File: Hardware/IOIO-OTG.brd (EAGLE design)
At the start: 68.6 x 30.5 mm, 51 parts, among them Q1 IRLML2244, Q2 2N7002PW, U1 PIC24FJ256GB206, U14 SWITCH_SPDT, U2 TPS6214X"", U3 VREG_MIC5216

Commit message: Consistency fixes
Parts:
- C10: device SparkFun-Passives:EIA3216 -> SparkFun-Capacitors:EIA3216
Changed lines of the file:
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@@
 <attribute name="VALUE" x="32.0997" y="20.221653125" size="0.4064" layer="27" rot="R45"/>
 </element>
-<element name="C10" library="SparkFun-Passives" package="EIA3216" value="10uF" x="38.1" y="21.59" smashed="yes" rot="R270">
+<element name="C10" library="SparkFun-Capacitors" package="EIA3216" value="10uF" x="38.1" y="21.59" smashed="yes" rot="R270">
 <attribute name="NAME" x="39.481" y="24.13" size="0.4064" layer="25" rot="R270"/>
 <attribute name="VALUE" x="39.432" y="21.182" size="0.4064" layer="27" rot="R270"/>

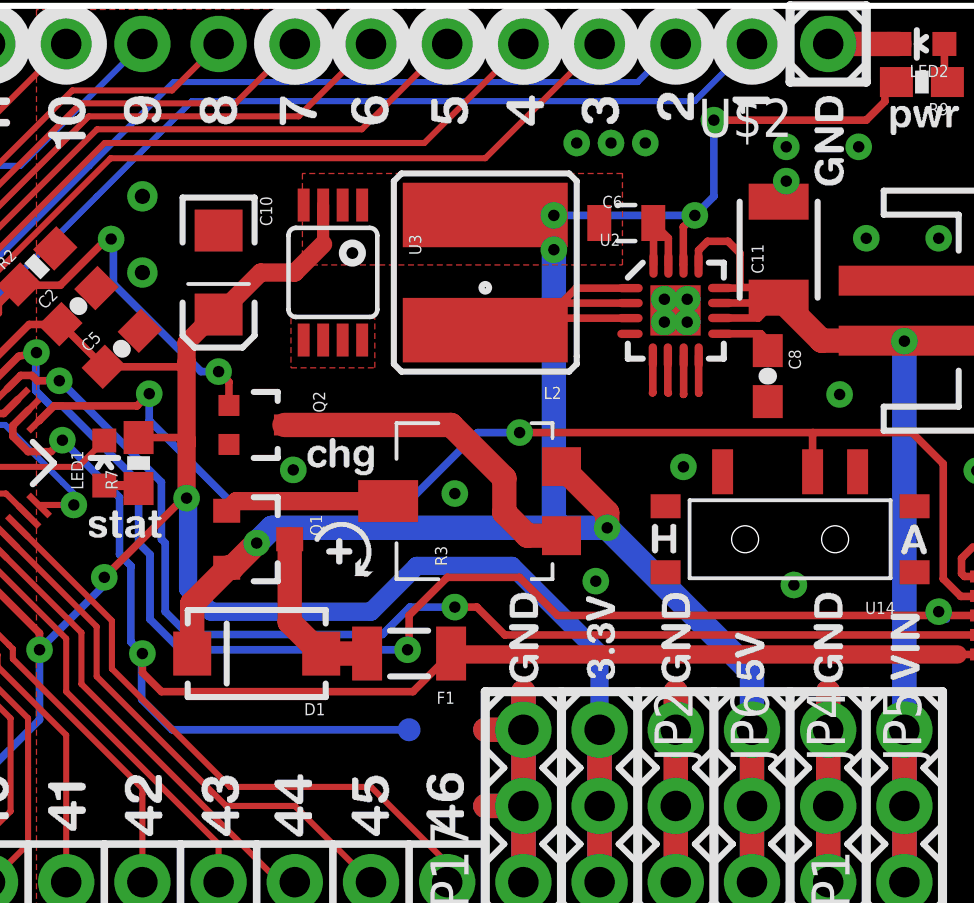
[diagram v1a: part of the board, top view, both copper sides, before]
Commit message: Final 6.5.0 inconsistency fixes
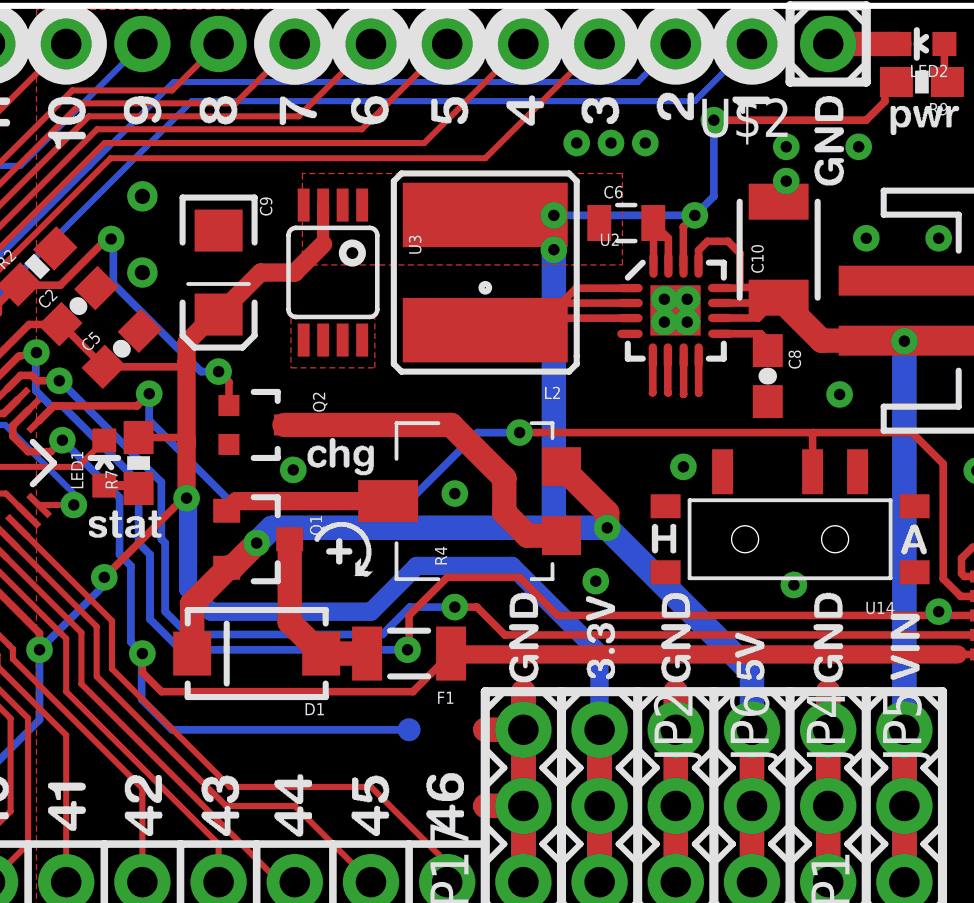
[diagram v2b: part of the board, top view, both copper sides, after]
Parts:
- removed C11: 10uF, SparkFun-Passives:1210
- added C9: 10uf, SparkFun-Capacitors:EIA3216
- C10: value 10uF -> 10uf; device SparkFun-Capacitors:EIA3216 -> SparkFun-Passives:1210
- C6: value 10uF -> 10uf
- D1: value B340A -> DIODE-SCHOTTKY_
- Q2: value 2N7002PW -> MOSFET-NCHANNEL2N7002PW"; device SparkFun-DiscreteSemi:SOT323 -> SparkFun-DiscreteSemi:SOT323_NOAT
- R4: value TS53YL502MR10 -> TRIMPOTSMD_STANDARD
- moved C10 18.7 mm to (56.8, 22.4), turned to 90 degrees
- renumbered R3 to R4
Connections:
- net 3.3V: now also C9.A; no longer C10.A
- net GND: now also C10.2, C9.C; no longer C10.C, C11.2
- net VIN: now also C10.1; no longer C11.1
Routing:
- net VIN: track 37.7 -> 38.7 mm

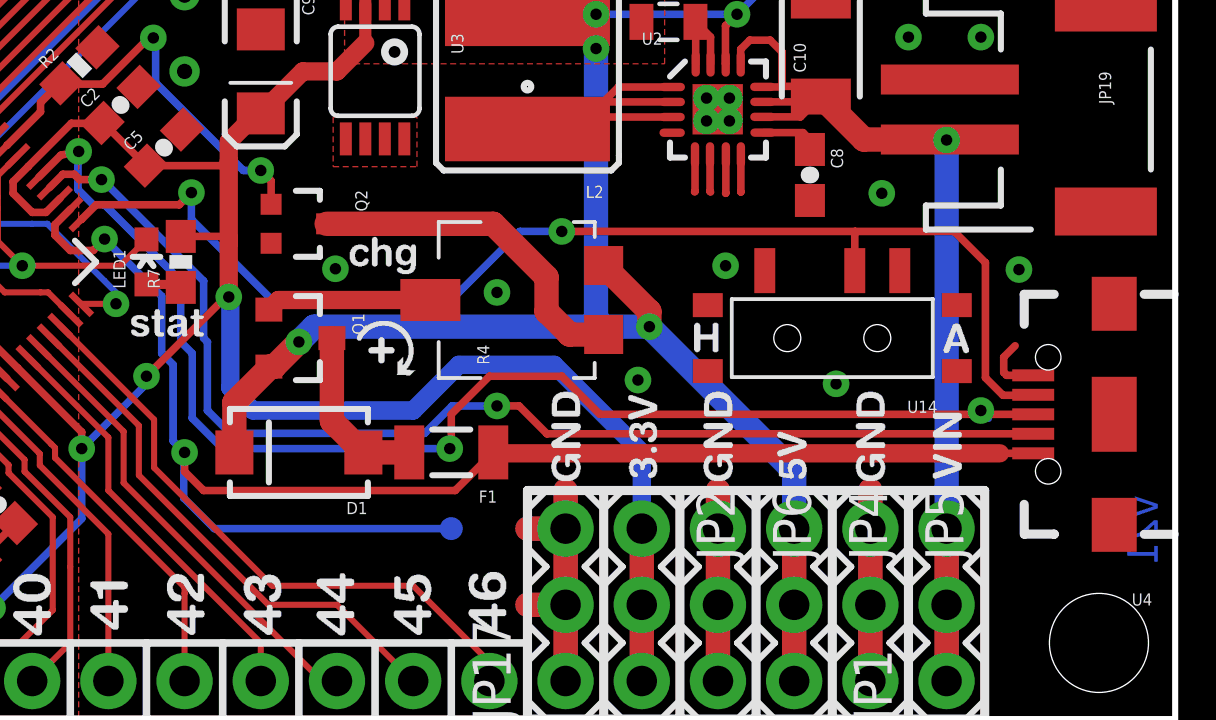
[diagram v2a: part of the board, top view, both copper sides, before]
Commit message: Added test-points
3 new test-points:
D+
D-
USBID
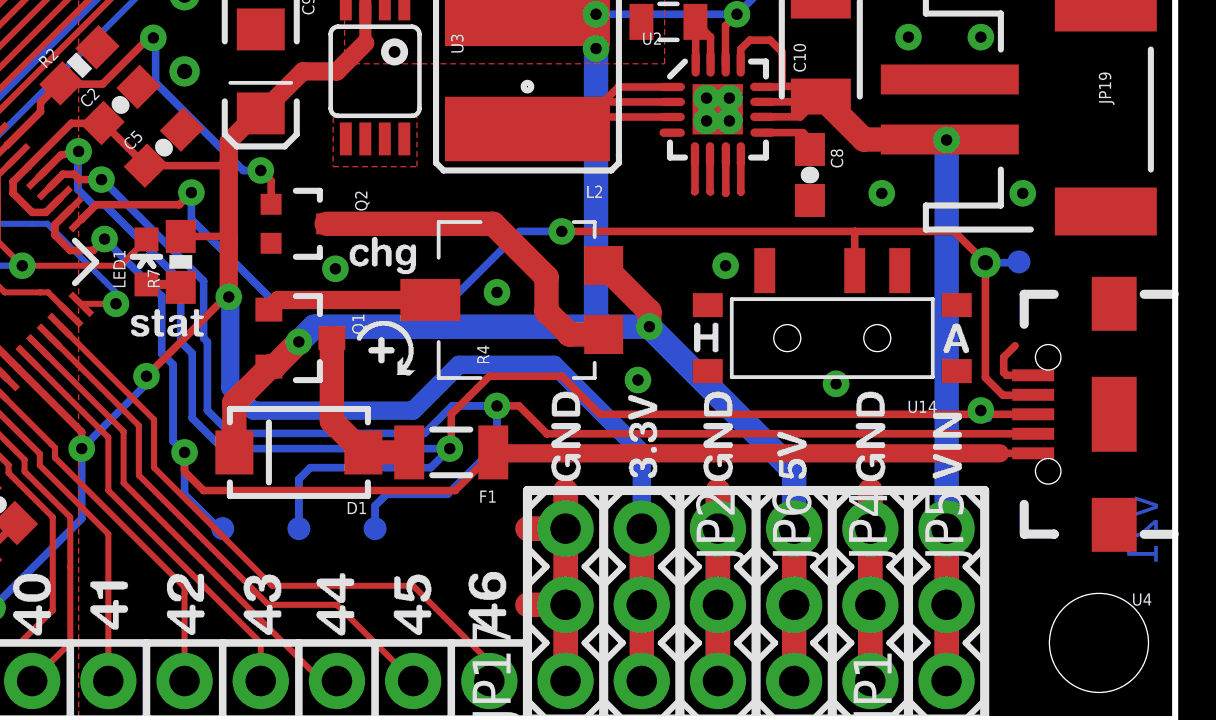
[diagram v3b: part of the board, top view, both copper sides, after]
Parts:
- added TP2, TP3, TP4: TEST-POINT3, SparkFun-Passives:PAD.03X.03
- moved TP1 7.62 mm to (36.8, 6.35)
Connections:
- net D+: now also TP3.P$1
- net D-: now also TP2.P$1
- net USBID: now also TP4.P$1
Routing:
- net VBUS: track 52.0 -> 44.2 mm
- net D+: track 43.4 -> 50.5 mm
- net D-: track 39.8 -> 46.7 mm
- net USBID: track 40.9 -> 42.0 mm, vias 2 -> 3
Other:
- board text added: "D+"
- board text added: "D-"
- board text added: "ID"
